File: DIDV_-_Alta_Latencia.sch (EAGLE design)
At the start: 117 parts, among them K201 G5L, Q101 BC817, Q201 BC817, Q202 BC817, Q203 BC807, Q204 BC817, Q205 BC807, Q206 FZT493, Q207 BC817, Q208 BC807, X101 RASPBERRYPI-B+-GPIO

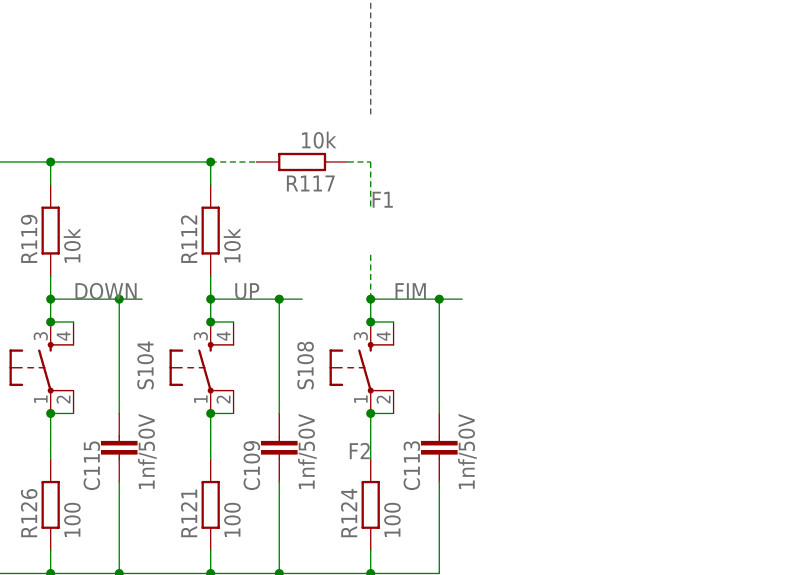
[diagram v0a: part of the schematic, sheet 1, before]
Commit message: Revisão 7:
-  Alterações necessárias para adequação às necessidades dos exemplos de controle que temos.
-  Revisão da forma de filtragem de sinais digitais
-  Algumas nomenclaturas ainda estão erradas, deverão ser corrigidas com o andamento da implementação.
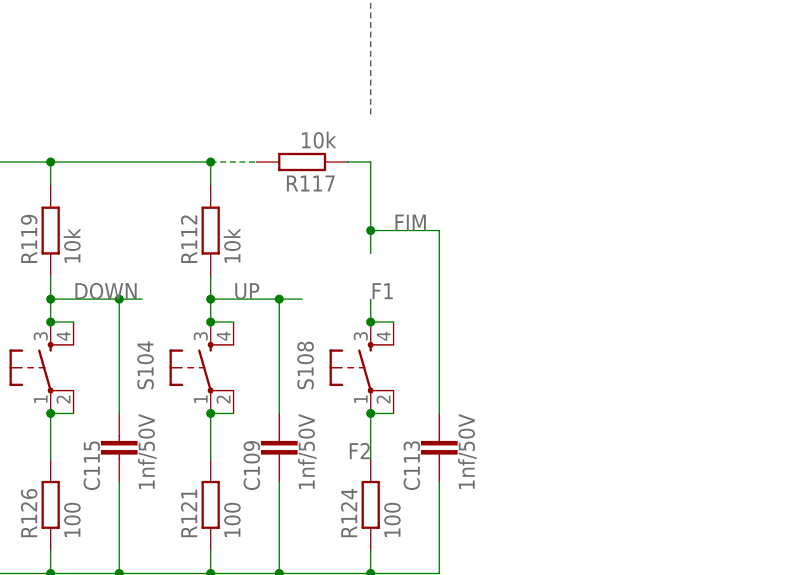
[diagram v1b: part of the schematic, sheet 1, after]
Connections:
- net F1: now also K201-A.NC, S108.3, S108.4; no longer K201-A.COM, R117.1
- net FIM: now also K201-A.COM, R117.1; no longer K201-A.NC, S108.3, S108.4
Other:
- note added: "07"
- note removed: "06"
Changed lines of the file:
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@@
 <setting verticaltext="up"/>
 </settings>
-<grid distance="0.1" unitdist="inch" unit="inch" style="lines" multiple="1" display="no" altdistance="0.01" altunitdist="inch" altunit="inch"/>
+<grid distance="0.1" unitdist="inch" unit="inch" style="lines" multiple="1" display="yes" altdistance="0.01" altunitdist="inch" altunit="inch"/>
 <layers>
 <layer number="1" name="Top" color="4" fill="1" visible="no" active="no"/>
@@
 <text x="203.2" y="29.464" size="1.778" layer="150" font="vector">Dispositivo de Interface para</text>
 <text x="210.82" y="26.162" size="1.778" layer="150" font="vector">Deficientes Visuais</text>
-<text x="250.698" y="10.16" size="2.54" layer="150" font="vector">06</text>
+<text x="250.698" y="10.16" size="2.54" layer="150" font="vector">07</text>
 <text x="198.12" y="43.18" size="2.54" layer="97" font="vector">Buzzer</text>
 <wire x1="127" y1="68.58" x2="144.78" y2="68.58" width="0.1524" layer="150" style="longdash"/>
@@
 </segment>
 <segment>
-<pinref part="S108" gate="S" pin="3"/>
-<pinref part="S108" gate="S" pin="4"/>
-<wire x1="127" y1="45.72" x2="129.54" y2="45.72" width="0.1524" layer="91"/>
-<junction x="127" y="45.72"/>
-<wire x1="127" y1="48.26" x2="127" y2="45.72" width="0.1524" layer="91"/>
-<wire x1="127" y1="48.26" x2="134.62" y2="48.26" width="0.1524" layer="91"/>
+<wire x1="127" y1="55.88" x2="134.62" y2="55.88" width="0.1524" layer="91"/>
 <pinref part="C113" gate="G$1" pin="1"/>
-<wire x1="134.62" y1="48.26" x2="137.16" y2="48.26" width="0.1524" layer="91"/>
-<wire x1="134.62" y1="35.56" x2="134.62" y2="48.26" width="0.1524" layer="91"/>
-<junction x="134.62" y="48.26"/>
-<label x="129.54" y="48.26" size="1.778" layer="95"/>
-<wire x1="127" y1="48.26" x2="127" y2="53.34" width="0.1524" layer="91" style="longdash"/>
-<junction x="127" y="48.26"/>
+<wire x1="134.62" y1="35.56" x2="134.62" y2="55.88" width="0.1524" layer="91"/>
+<pinref part="R117" gate="G$1" pin="1"/>
+<wire x1="124.46" y1="63.5" x2="127" y2="63.5" width="0.1524" layer="91"/>
+<wire x1="127" y1="63.5" x2="127" y2="55.88" width="0.1524" layer="91"/>
+<wire x1="127" y1="55.88" x2="127" y2="53.34" width="0.1524" layer="91"/>
+<junction x="127" y="55.88"/>
+<label x="129.54" y="55.88" size="1.778" layer="95"/>
 </segment>
 </net>
@@
 </segment>
 </net>
-<net name="F1" class="0">
-<segment>
-<pinref part="R117" gate="G$1" pin="1"/>
-<wire x1="124.46" y1="63.5" x2="127" y2="63.5" width="0.1524" layer="91" style="longdash"/>
-<wire x1="127" y1="63.5" x2="127" y2="58.42" width="0.1524" layer="91" style="longdash"/>
-<label x="127" y="58.42" size="1.778" layer="95"/>
-</segment>
-</net>
 <net name="N$28" class="0">
 <segment>
@@
 </segment>
 </net>
+<net name="F1" class="0">
+<segment>
+<pinref part="S108" gate="S" pin="4"/>
+<pinref part="S108" gate="S" pin="3"/>
+<wire x1="127" y1="45.72" x2="129.54" y2="45.72" width="0.1524" layer="91"/>
+<wire x1="127" y1="45.72" x2="127" y2="48.26" width="0.1524" layer="91"/>
+<junction x="127" y="45.72"/>
+<label x="127" y="48.26" size="1.778" layer="95"/>
+</segment>
+</net>
 </nets>
 </sheet>
@@
 <text x="203.2" y="29.464" size="1.778" layer="150" font="vector">Dispositivo de Interface para</text>
 <text x="210.82" y="26.162" size="1.778" layer="150" font="vector">Deficientes Visuais</text>
-<text x="250.698" y="10.16" size="2.54" layer="150" font="vector">06</text>
+<text x="250.698" y="10.16" size="2.54" layer="150" font="vector">07</text>
 <text x="10.16" y="96.52" size="2.54" layer="97" font="vector">Conversor_PICProgrammer</text>
 <wire x1="7.62" y1="93.98" x2="7.62" y2="172.72" width="0.1524" layer="97" style="longdash"/>
@@
 </segment>
 </net>
-<net name="F1" class="0">
-<segment>
-<pinref part="K201" gate="-A" pin="COM"/>
-<wire x1="241.3" y1="81.28" x2="241.3" y2="76.2" width="0.1524" layer="91"/>
-<label x="241.3" y="76.2" size="1.778" layer="95"/>
-</segment>
-</net>
 <net name="TE" class="0">
 <segment>
@@
 </segment>
 </net>
-<net name="FIM" class="0">
-<segment>
-<pinref part="K201" gate="-A" pin="NC"/>
-<wire x1="246.38" y1="88.9" x2="251.46" y2="88.9" width="0.1524" layer="91"/>
-<label x="248.92" y="88.9" size="1.778" layer="95"/>
-</segment>
-</net>
 <net name="F2" class="0">
 <segment>
@@
 </segment>
 </net>
+<net name="FIM" class="0">
+<segment>
+<pinref part="K201" gate="-A" pin="COM"/>
+<wire x1="241.3" y1="81.28" x2="241.3" y2="76.2" width="0.1524" layer="91"/>
+<label x="241.3" y="76.2" size="1.778" layer="95"/>
+</segment>
+</net>
+<net name="F1" class="0">
+<segment>
+<pinref part="K201" gate="-A" pin="NC"/>
+<wire x1="246.38" y1="88.9" x2="251.46" y2="88.9" width="0.1524" layer="91"/>
+<label x="246.38" y="86.36" size="1.778" layer="95"/>
+</segment>
+</net>

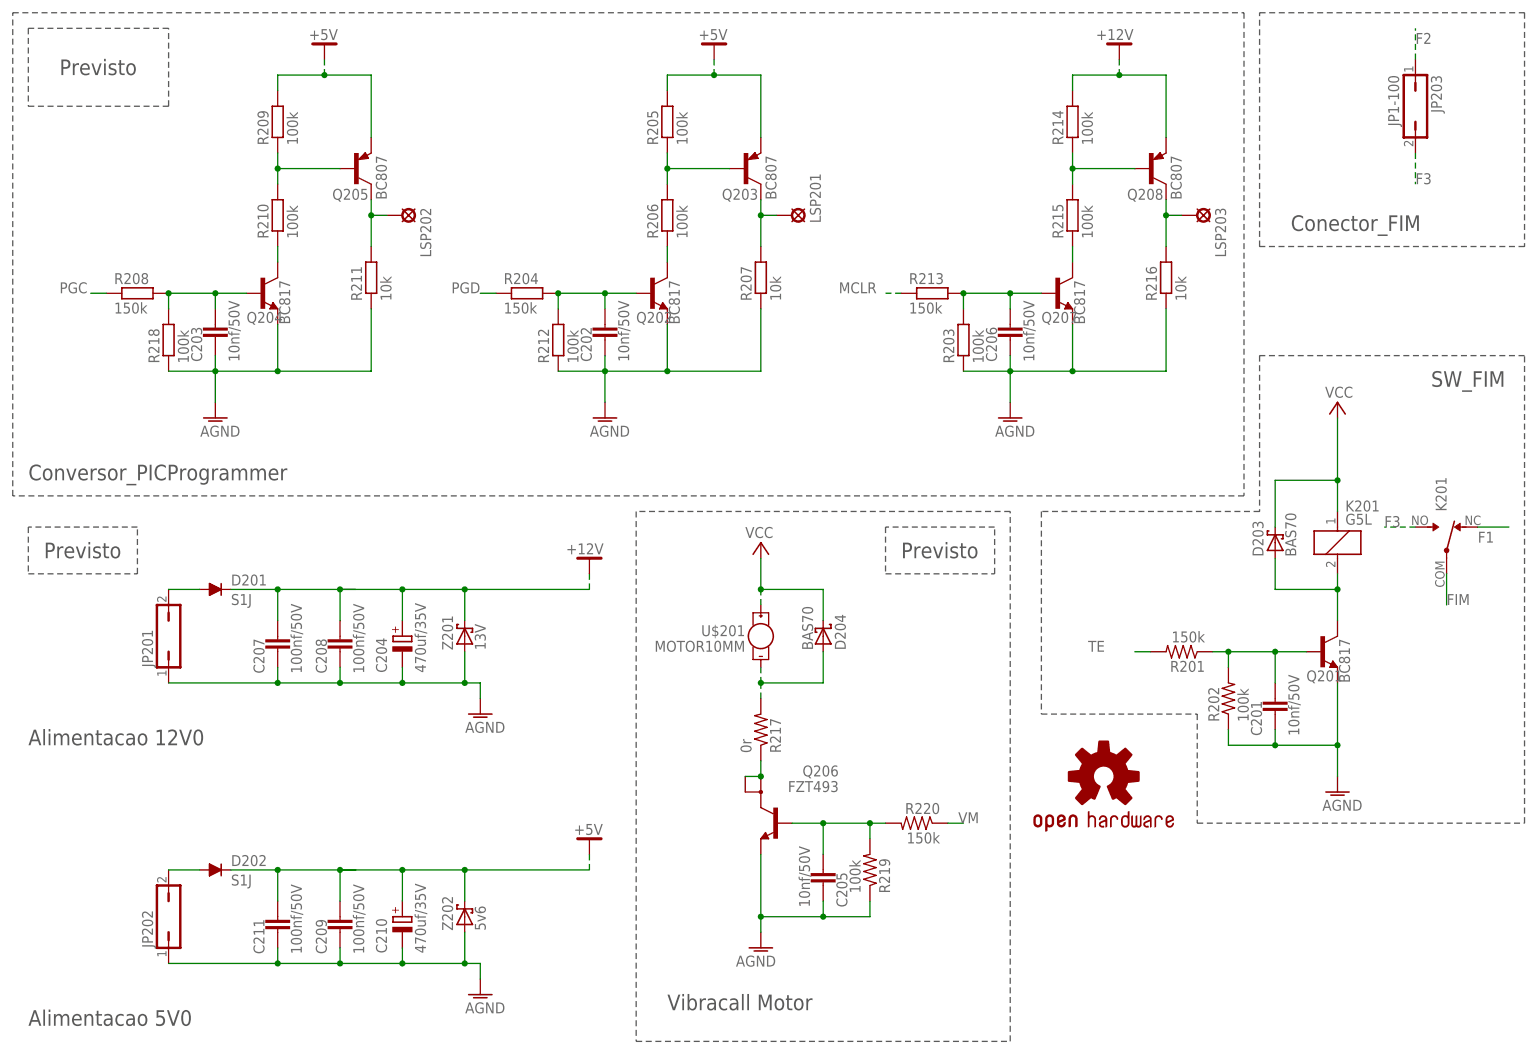
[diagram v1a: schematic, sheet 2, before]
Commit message: Revisão 8:
-  Add Circuito Buck
-  Alterações funcionais
-   Inserção dos primeiros boards
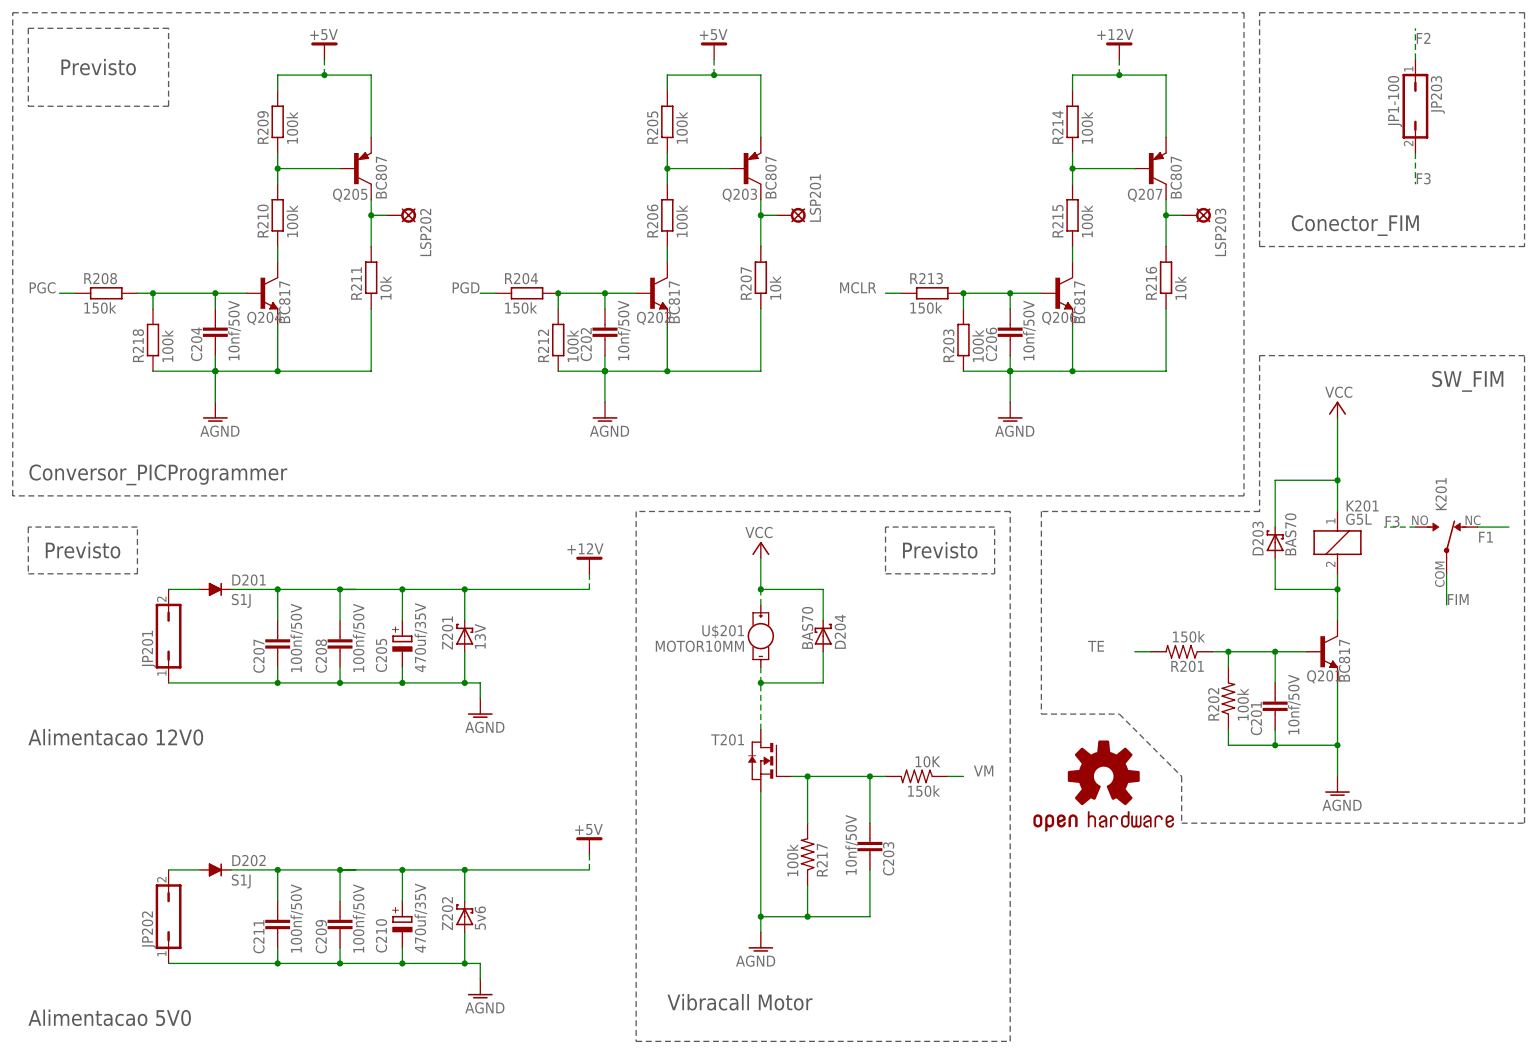
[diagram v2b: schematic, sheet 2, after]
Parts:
- removed Q208: BC807, transistor-pnp:BC807-40SMD
- removed R219: 100k, rcl:R-US_R1206
- removed R220: 150k, rcl:R-US_R1206
- added 10K: 150k, rcl:R-US_R1206
- added T201: (no value), PG-TDSON-8:BSC067N06LS3_G_PG-TDSON-8
- C204: value 470uf/35V -> 10nf/50V; device rcl:CPOL-EU140CLH-1014 -> rcl:C-EUC0603K
- C205: value 10nf/50V -> 470uf/35V; device rcl:C-EUC0603K -> rcl:CPOL-EU140CLH-1014
- Q206: value FZT493 -> BC817; device zetex:FZT493 -> transistor-npn:BC817-16LT1SMD
- Q207: value BC817 -> BC807; device transistor-npn:BC817-16LT1SMD -> transistor-pnp:BC807-40SMD
- R217: value 0r -> 100k
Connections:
- removed net N$45: Q206.C1, Q206.C2, R217.1
- net +12V: now also C205.+, Q207.E; no longer C204.+, Q208.E
- net AGND: now also C204.2, C205.-, R217.1, T201.S; no longer C204.-, C205.2, Q207.E, R219.1
- net N$1: now also 10K.2, C203.1, R217.2, T201.G; no longer C205.1, Q206.B, R219.2, R220.2
- net N$2: now also T201.D; no longer R217.2
- net N$30: now also C204.1; no longer C203.1
- net N$37: now also Q206.C; no longer Q207.C
- net N$38: now also Q206.B; no longer Q207.B
- net N$39: now also Q207.B; no longer Q208.B
- net N$40: now also Q207.C; no longer Q208.C
- net VM: now also 10K.1; no longer R220.1
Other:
- note added: "08"
- note removed: "07"
- moved on the sheet: C203, Q206, R208, R217, R218

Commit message: Revisão 9
- Corrigidos algumas falhas de ligação
- Implementação com VPRG dos TLCs via Hardware
- Inserção do cálculo do Riref

Obs. Se somente a criação de boards, não será incrementado. No caso, se criado um board novo board vou subir para 9.1 e assim por diante.
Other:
- note added: "09"
- note removed: "08"
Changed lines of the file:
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@@
 <text x="203.2" y="29.464" size="1.778" layer="150" font="vector">Dispositivo de Interface para</text>
 <text x="210.82" y="26.162" size="1.778" layer="150" font="vector">Deficientes Visuais</text>
-<text x="250.698" y="10.16" size="2.54" layer="150" font="vector">08</text>
+<text x="250.698" y="10.16" size="2.54" layer="150" font="vector">09</text>
 <text x="198.12" y="43.18" size="2.54" layer="97" font="vector">Buzzer</text>
 <wire x1="127" y1="68.58" x2="144.78" y2="68.58" width="0.1524" layer="150" style="longdash"/>
@@
 <text x="203.2" y="29.464" size="1.778" layer="150" font="vector">Dispositivo de Interface para</text>
 <text x="210.82" y="26.162" size="1.778" layer="150" font="vector">Deficientes Visuais</text>
-<text x="250.698" y="10.16" size="2.54" layer="150" font="vector">08</text>
+<text x="250.698" y="10.16" size="2.54" layer="150" font="vector">09</text>
 <text x="10.16" y="96.52" size="2.54" layer="97" font="vector">Conversor_PICProgrammer</text>
 <wire x1="7.62" y1="93.98" x2="7.62" y2="172.72" width="0.1524" layer="97" style="longdash"/>

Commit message: Revisão 10
Revisão representa o estado final do projeto, alterações agora somente referentes a valores de componentes e adaptações se e somente se não existir a possibilidade de manobras via software.

Placas nas dimensões e condições as quais foram submetidas a cotação para confecção em local especializado.
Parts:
- removed 10K: 150k, rcl:R-US_R1206
- removed C201, C202, C203, C204, C206: 10nf/50V, rcl:C-EUC0603K
- removed C205, C210: 470uf/35V, rcl:CPOL-EU140CLH-1014
- removed C207, C208, C209, C211: 100nf/50V, rcl:C-EUC0805
- removed D201, D202: S1J, diode:FS1J
- removed D203, D204: BAS70, diode:BAS40
- removed JP201, JP202: (no value), jumper:JP1Q
- removed JP203: JP1-100, jumpers:JP1-100
- removed K201: G5L, relay:G5L
- removed LOGO201: OSHW-LOGOM, SparkFun-Aesthetics:OSHW-LOGOM
- removed LSP201, LSP202, LSP203: LSP10, solpad:LSP10
- removed Q201, Q202, Q204, Q206: BC817, transistor-npn:BC817-16LT1SMD
- removed Q203, Q205, Q207: BC807, transistor-pnp:BC807-40SMD
- removed R201: 150k, rcl:R-US_R0603
- removed R202: 100k, rcl:R-US_R0603
- removed R203, R205, R206, R209, R210, R212, R214, R215, R218: 100k, rcl:R-EU_R0603
- removed R204, R208, R213: 150k, rcl:R-EU_R0603
- removed R207, R211, R216: 10k, rcl:R-EU_R0603
- removed R217: 100k, rcl:R-US_R1206
- removed T201: (no value), PG-TDSON-8:BSC067N06LS3_G_PG-TDSON-8
- removed U$201: MOTOR10MM, SparkFun-Electromechanical:MOTOR10MM
- removed Z201: 13V, diode:BAS70
- removed Z202: 5v6, diode:BAS70
- added C118, C119, C120, C122, C123, C124: 1nf/50V, rcl:C-EUC0603K
- added C121: 10nf/50V, rcl:C-EUC0603K
- added D102, D103: S1J, diode:FS1J
- added D104: BAS70, diode:BAS40
- added JP101, JP102: (no value), jumper:JP1QY
- added Q102: BC817, transistor-npn:BC817-16LT1SMD
- added R129: 1k15, rcl:R-US_R0805
- added R130: 100, rcl:R-US_R0603
- added U$101: MOTOR10MM, SparkFun-Electromechanical:MOTOR10MM
- added Z101: 13V, diode:BAS70
- added Z102: 5v6, diode:BAS70
- C101: value 10nf/50V -> 100nf/50V; device rcl:C-EUC0603K -> rcl:C-EUC0805
- C102, C106: value 1nf/50V -> 100nf/50V; device rcl:C-EUC0603K -> rcl:C-EUC0805
- C103: device rcl:C-EUC0603K -> rcl:C-EUC0805
- C108, C110: value 1nf/50V -> 470uf/35V; device rcl:C-EUC0603K -> rcl:CPOL-EU140CLH-1014
- C111, C116: value 1nf/50V -> 10nf/50V
- C112: value 10nf/50V -> 1nf/50V
- LOGO101: value OSHW-LOGOM -> OSHW-LOGOL; device SparkFun-Aesthetics:OSHW-LOGOM -> OpenHW_BOT:OSHW-LOGOL
- R101: value 10k -> 1k15; device rcl:R-EU_R0603 -> rcl:R-US_R0805
- R102: value 10k -> 1k; device rcl:R-EU_R0603 -> rcl:R-US_R0805
- R103, R105, R106, R108, R112, R114, R117, R121, R123, R124, R125, R126, R127: device rcl:R-EU_R0603 -> rcl:R-US_R0603
- R104, R107, R109, R110, R111, R113: value 100 -> 10k; device rcl:R-EU_R0603 -> rcl:R-US_R0603
- R115: value 150k -> 100; device rcl:R-EU_R0603 -> rcl:R-US_R0603
- R116: value 100k -> 100; device rcl:R-EU_R0603 -> rcl:R-US_R0603
- R118, R119, R120, R122: value 10k -> 100; device rcl:R-EU_R0603 -> rcl:R-US_R0603
- R128: value 100 -> 1k; device rcl:R-EU_R0603 -> rcl:R-US_R0805
- S101, S102, S103, S104, S105, S106, S108, S109, S110, S111, S112, S113: value (none) -> DTS-3; device SparkFun-Electromechanical:TAC_SWITCHPTH -> switch-tact:DTS-3
- S107: value (none) -> DTS-3; device SparkFun-Electromechanical:TAC_SWITCHSMD -> switch-tact:DTS-3
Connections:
- removed net +5V: C209.1, C210.+, C211.1, D202.C, Q203.E, Q205.E, R205.2, R209.2, Z202.C
- removed net AGND: C101.2, C102.2, C103.2, C104.2, C105.2, C106.2, C108.2, C109.2, C110.2, C111.2, C112.2, C113.2, C114.2, C115.2, C116.2, C117.2, C201.2, C202.2, C203.2, C204.2, C205.-, C206.2, C207.2, C208.2, C209.2, C210.-, C211.2, JP201.1, JP202.1, Q101.E, Q201.E, Q202.E, Q204.E, Q206.E, R104.1, R107.1, R109.1, R110.1, R111.1, R113.1, R116.1, R121.1, R123.1, R124.1, R125.1, R126.1, R127.1, R128.1, R202.1, R203.1, R207.1, R211.1, R212.1, R216.1, R217.1, R218.1, T201.S, X101.GND@14, X101.GND@20, X101.GND@25, X101.GND@30, X101.GND@34, X101.GND@39, X101.GND@6, X101.GND@9, Z201.A, Z202.A
- removed net F1: K201-A.NC, S108.3, S108.4
- removed net F3: JP203.2, K201-A.NO
- removed net MCLR: R213.1
- removed net N$1: 10K.2, C203.1, R217.2, T201.G
- removed net N$108: D203.A, K201C.2, Q201.C
- removed net N$2: D204.A, T201.D, U$201.-
- removed net N$34: C202.1, Q202.B, R204.2, R212.2
- removed net N$35: Q203.B, R205.1, R206.2
- removed net N$36: LSP201.MP, Q203.C, R207.2
- removed net N$37: Q206.C, R215.1
- removed net N$38: C206.1, Q206.B, R203.2, R213.2
- removed net N$39: Q207.B, R214.1, R215.2
- removed net N$40: LSP203.MP, Q207.C, R216.2
- removed net N$41: D201.A, JP201.2
- removed net N$42: C201.1, Q201.B, R201.1, R202.2
- removed net N$43: D202.A, JP202.2
- removed net PGC: R208.1
- removed net PGD: R204.1
- new net GND: C101.2, C102.2, C103.2, C104.2, C105.2, C106.2, C107.2, C108.-, C109.2, C110.-, C111.2, C112.2, C113.2, C114.2, C115.2, C117.2, C118.2, C119.2, C120.2, C122.2, C123.2, C124.2, JP101.1, JP102.1, Q101.E, R115.1, R116.1, R118.1, R119.1, R120.1, R121.1, R122.1, R123.1, R124.1, R125.1, R126.1, R127.1, R128.1, R130.1, X101.GND@14, X101.GND@20, X101.GND@25, X101.GND@30, X101.GND@34, X101.GND@39, X101.GND@6, X101.GND@9, Z101.A, Z102.A
- net +12V: now also C101.1, C103.1, C108.+, C116.1, D102.C, D104.C, SG101.1, Z101.C; no longer C107.1, C205.+, C207.1, C208.1, D101.C, D201.C, Q207.E, R214.2, SG101.2, Z201.C
- net +3V3: now also C107.1, C111.1, R104.2, R107.2, R109.2, R110.2, R111.2, R113.2; no longer C101.1, C104.1, R101.2, R102.2, R118.2, R119.2, R120.2, R122.2
- net B01: now also C115.1, R103.1, S101.2; no longer C110.1, R105.1, S105.3, S105.4
- net B02: now also C112.1, R104.1, S102.2; no longer C105.1, R108.1, S109.3, S109.4
- net B03: now also C114.1, R105.1, S103.2; no longer C108.1, R102.1, S102.3, S102.4
- net B04: now also C109.1, S104.2; no longer C103.1, S106.3, S106.4
- net B05: now also C113.1, R107.1, S105.2; no longer C106.1, R101.1, S101.3, S101.4
- net B06: now also C105.1, R108.1, S106.2; no longer C102.1, R103.1, S103.3, S103.4
- net BACKSPACE: now also C120.1, R110.1, S108.2; no longer C114.1, R118.1, S110.3, S110.4
- net BUZZER: now also R101.2; no longer R115.1
- net DOWN: now also C122.1, R113.1, S111.2; no longer C115.1, R119.1, S111.3, S111.4
- net ENTER: now also C124.1, R109.1, S107.2; no longer C117.1, R122.1, S113.3, S113.4
- net ESC: now also C123.1, R111.1, S109.2; no longer C116.1, R120.1, S112.3, S112.4
- net ESPAÇO: now also C118.1, R112.1, S110.2; no longer C111.1, R114.1, S107.3, S107.4
- net F2: now also R118.2, S113.1; no longer JP203.1, R124.2, S108.1, S108.2
- net FIM: now also C119.1, S113.2; no longer C113.1, K201-A.COM
- net N$14: now also C116.2, D104.A, Q102.C, SG101.2; no longer C107.2, D101.A, Q101.C, SG101.1
- net N$15: now also C121.1, Q102.B, R101.1, R102.2; no longer C112.1, Q101.B, R115.2, R116.2
- net N$16: now also R130.2, S101.1; no longer R113.2, S105.1, S105.2
- net N$17: now also R121.2, S106.1; no longer R104.2, S103.1, S103.2
- net N$18: now also R126.2, S105.1; no longer R110.2, S101.1, S101.2
- net N$19: now also R123.2, S104.1; no longer R107.2, S106.1, S106.2
- net N$20: now also R127.2, S103.1; no longer R111.2, S102.1, S102.2
- net N$21: now also R125.2, S102.1; no longer R109.2, S109.1, S109.2
- net N$22: now also R124.2, S107.1; no longer R128.2, S113.1, S113.2
- net N$23: now also R115.2, S112.1; no longer R121.2, S104.1, S104.2
- net N$24: now also R120.2; no longer R126.2, S111.2
- net N$25: now also R116.2, S110.1; no longer R123.2, S107.1, S107.2
- net N$26: now also R122.2, S109.1; no longer R127.2, S112.1, S112.2
- net N$27: now also R119.2, S108.1; no longer R125.2, S110.1, S110.2
- net N$29: now also C104.1, Q101.B, R128.2, R129.2; no longer Q204.C, R210.1
- net N$30: now also D101.A, Q101.C, U$101.-; no longer C204.1, Q204.B, R208.2, R218.2
- net N$31: now also D102.A, JP101.2; no longer Q205.B, R209.1, R210.2
- net N$32: now also D103.A, JP102.2; no longer LSP202.MP, Q205.C, R211.2
- net N$33: now also C121.2, Q102.E, R102.1; no longer Q202.C, R206.1
- net TE: no longer R201.2
- net UP: now also C117.1, R114.1, S112.2; no longer C109.1, R112.1, S104.3, S104.4
- net VCC: now also C102.1, C106.1, C110.+, D101.C, D103.C, U$101.+, Z102.C; no longer D203.C, D204.C, K201C.1, U$201.+
- net VM: now also R129.1; no longer 10K.1
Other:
- note added: "10"
- note added: "Desacoplamento"
- note removed: "09"
- note removed: "Conector_FIM"
- note removed: "Conversor_PICProgrammer"
- note removed: "SW_FIM"
